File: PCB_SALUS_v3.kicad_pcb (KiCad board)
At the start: 2 copper layers, 100 x 100 mm, 85 parts, among them J1 Debug_U0, J10 RELES_2, J11 Throttle, J12 I2C_EXT1, J13 I2C_EXT2, J14 S_HALL, J15 RF_PPM, J16 USB_NATIVO, J17 SERVO2, J18 SERVO1, J19 +7V_IN, J2 S_GIRO, J20 3V_IN, J3 RS485, J4 Uart1, J5 5V_IN, J6 IBT_2, J7 FC1, J8 FC2, J9 RELES_1, U1 AMS1117CD-3.3, U2 SP3485EN, U4 BMI088, U5 74HC595, U6 ULN2003A, U7 LM358, U8 ESP32-S3-WROOM-1

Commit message: fixes
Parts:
- D1: value SM712_SOT23 -> SM712-02HTG
- moved D1 4.22 mm to (61.6, 117.8)
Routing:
- net /ESP32/RS485_A: track 11.2 -> 13.9 mm
- net /ESP32/RS485_B: track 14.6 -> 13.2 mm
- net GND: vias 11 -> 19

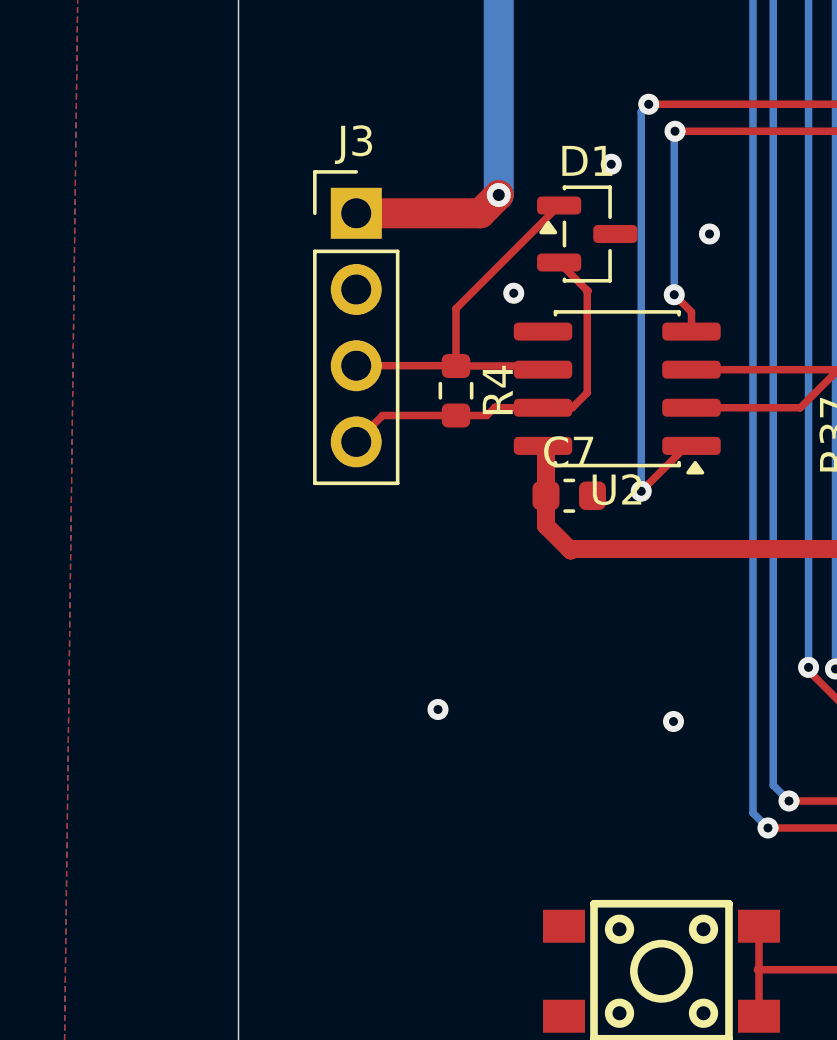
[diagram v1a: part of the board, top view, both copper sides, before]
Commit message: add second header for rs485
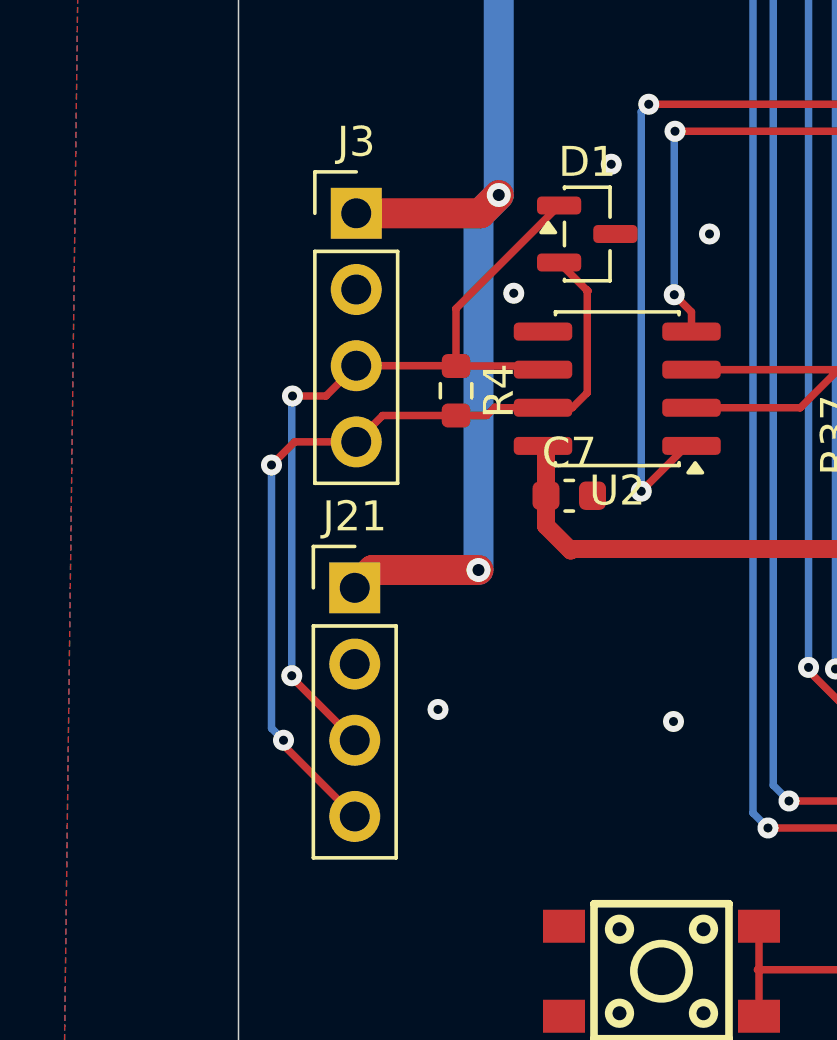
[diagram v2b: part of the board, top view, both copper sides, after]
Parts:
- added J21: RS485, Connector_PinHeader_2.54mm:PinHeader_1x04_P2.54mm_Vertical, F.Cu at (53.9, 129.6)
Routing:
- net +5V: track 264.9 -> 282.0 mm, vias 10 -> 11
- net /ESP32/RS485_B: track 13.2 -> 29.2 mm, vias 0 -> 2
- net /ESP32/RS485_A: track 13.9 -> 28.8 mm, vias 0 -> 2

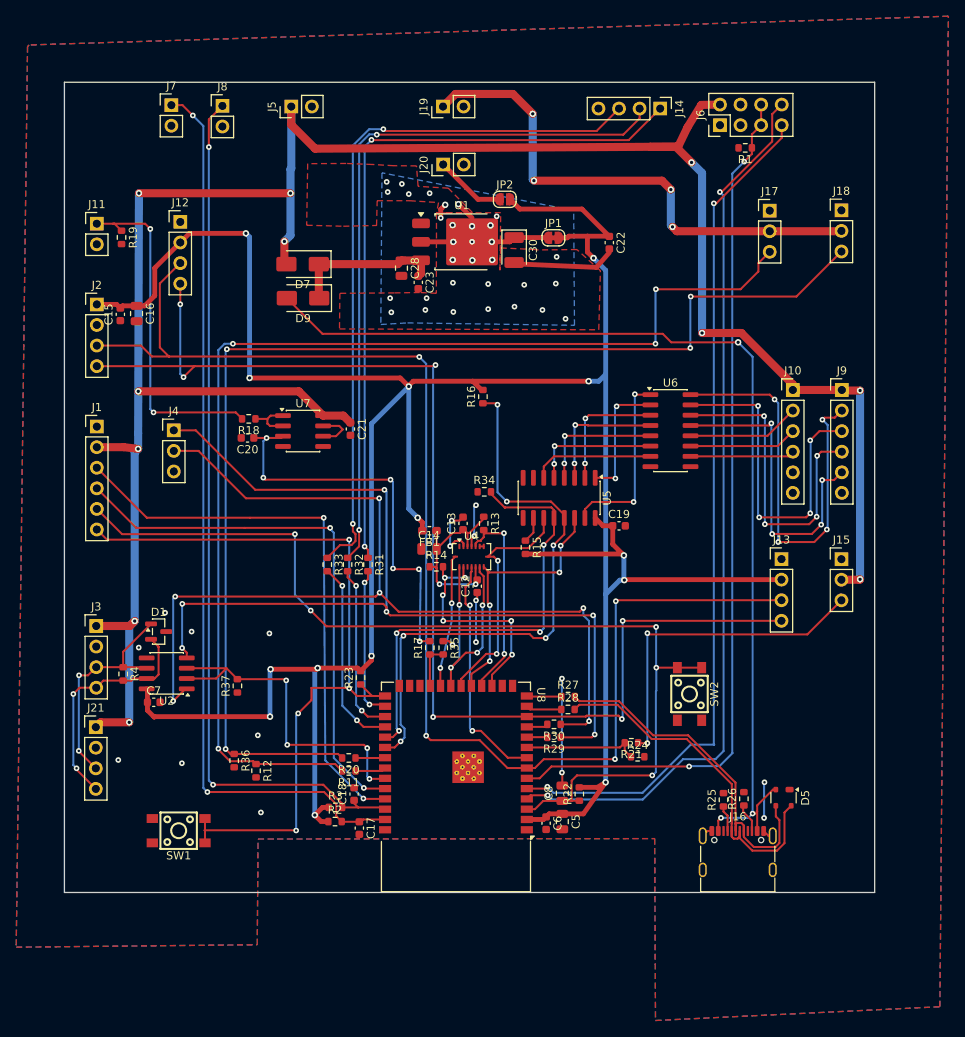
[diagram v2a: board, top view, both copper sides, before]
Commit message: vias de gnd y pin header de GPIOS sobrantes
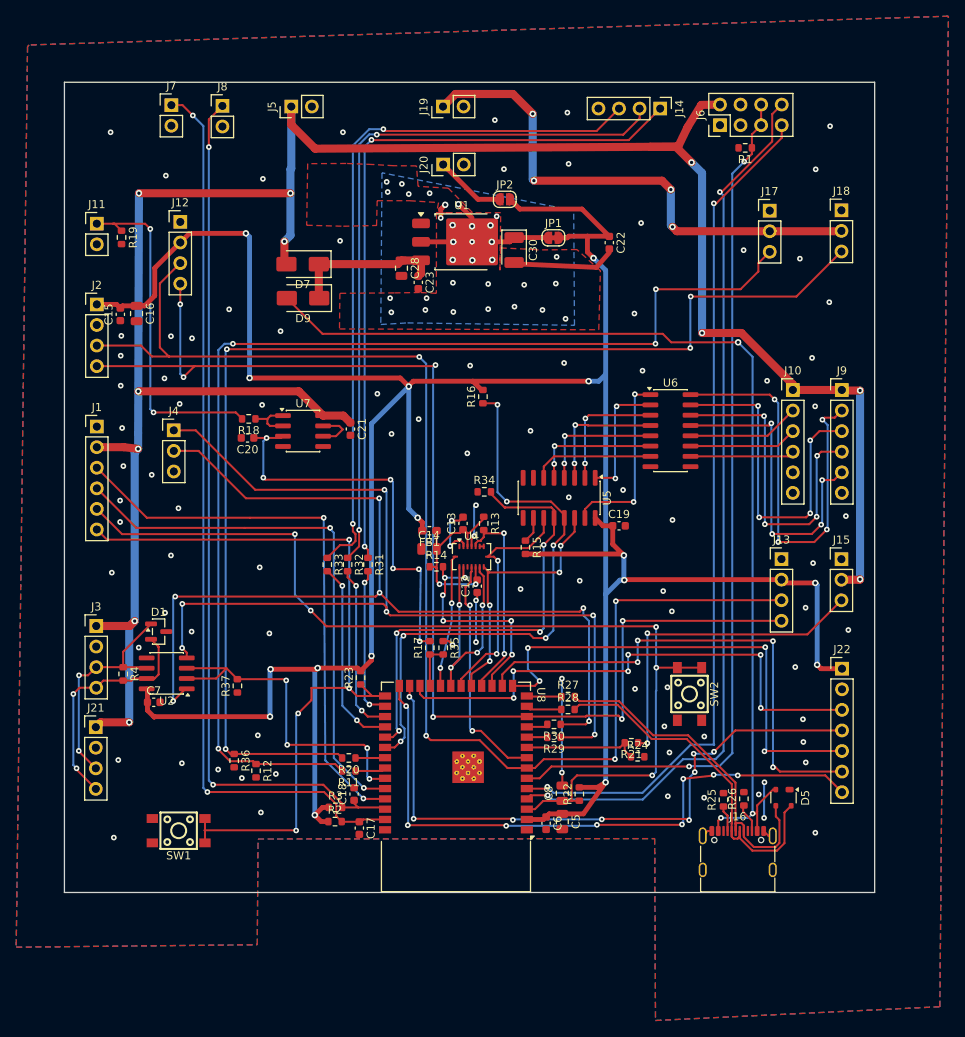
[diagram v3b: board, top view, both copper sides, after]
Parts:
- added J22: Conn_01x07, Connector_PinHeader_2.54mm:PinHeader_1x07_P2.54mm_Vertical, F.Cu at (146.0, 122.4)
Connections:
- U8 pad 15: unconnected-(U8-IO3-Pad15) -> /ESP32/IO3
- U8 pad 16: unconnected-(U8-IO46-Pad16) -> /ESP32/IO46
- U8 pad 24: unconnected-(U8-IO47-Pad24) -> /ESP32/IO47
- U8 pad 25: unconnected-(U8-IO48-Pad25) -> /ESP32/IO48
- U8 pad 26: unconnected-(U8-IO45-Pad26) -> /ESP32/IO45
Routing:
- net /ESP32/IO48: track 0.00 -> 78.9 mm, vias 0 -> 8
- net /ESP32/IO45: track 0.00 -> 77.9 mm, vias 0 -> 8
- net /ESP32/IO47: track 0.00 -> 65.4 mm, vias 0 -> 6
- net /ESP32/IO46: track 0.00 -> 62.5 mm, vias 0 -> 4
- net /ESP32/IO3: track 0.00 -> 60.2 mm, vias 0 -> 4
- net +3.3V: track 351.9 -> 369.7 mm, vias 14 -> 16
- net GND: vias 19 -> 93

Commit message: Mejora serigrafia profesional SALUS v3
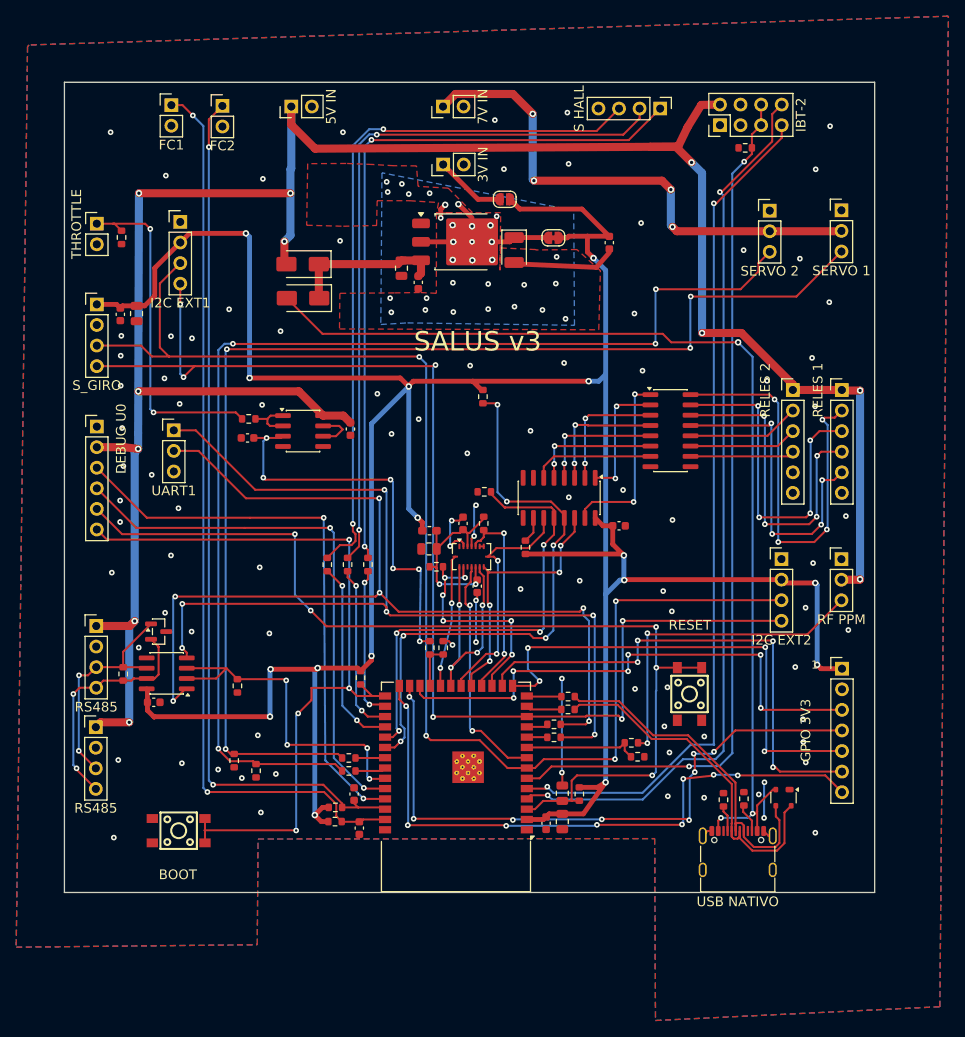
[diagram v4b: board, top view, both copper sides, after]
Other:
- board text added: "1"
- board text added: "3V IN"
- board text added: "5V IN"
- board text added: "7V IN"
- board text added: "BOOT"
- board text added: "DEBUG U0"
- board text added: "GPIO 3V3"
- board text added: "I2C EXT1"
- board text added: "I2C EXT2"
- board text added: "IBT-2"
- board text added: "RELES 1"
- board text added: "RELES 2"
- board text added: "RESET"
- board text added: "RF PPM"
- board text added: "S HALL"
- board text added: "SALUS v3"
- board text added: "SERVO 1"
- board text added: "SERVO 2"
- board text added: "THROTTLE"
- board text added: "UART1"
- board text added: "USB NATIVO"

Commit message: Identifica pines criticos de conectores
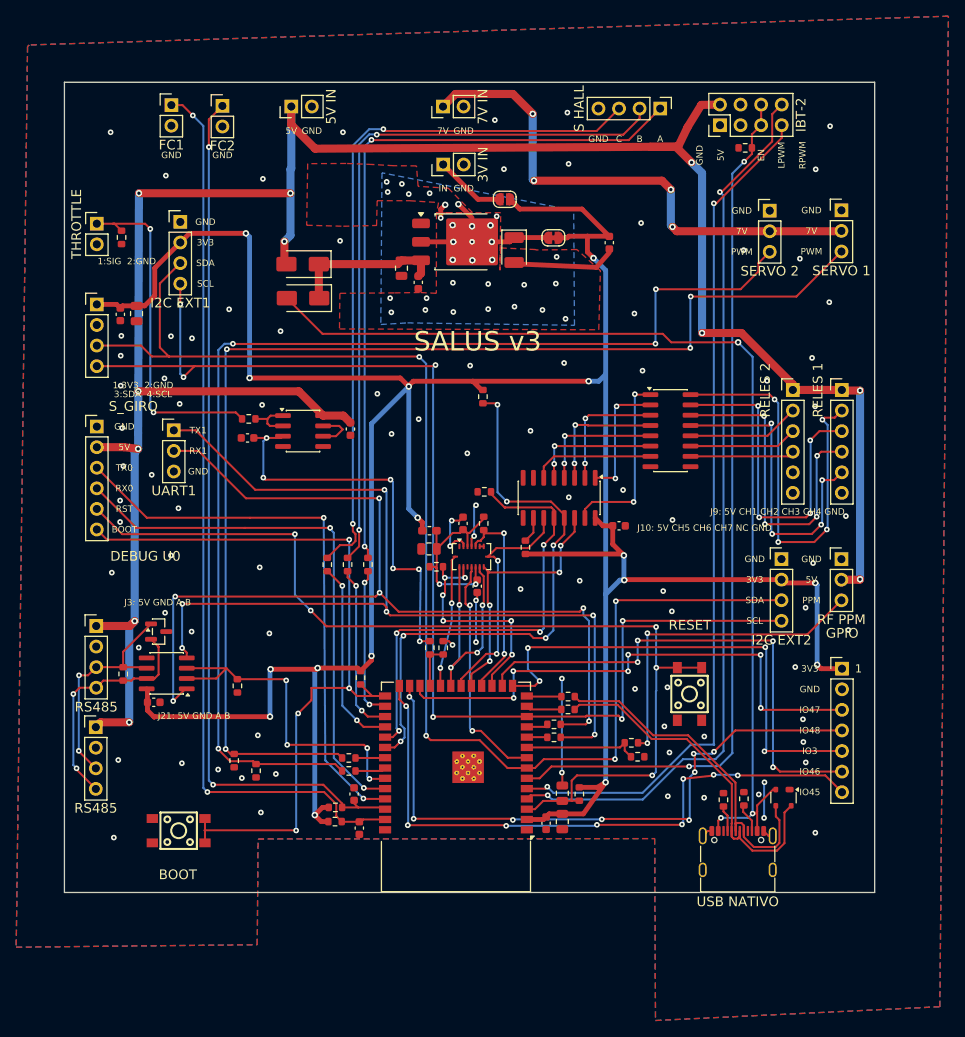
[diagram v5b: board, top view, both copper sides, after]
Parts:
- J22: value Conn_01x07 -> GPIOS_AUX
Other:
- board text added: "1:3V3 2:GND"
- board text added: "1:SIG 2:GND"
- board text added: "3:SDA 4:SCL"
- board text added: "3V3"
- board text added: "5V"
- board text added: "7V"
- board text added: "A"
- board text added: "B"
- board text added: "C"
- board text added: "EN"
- board text added: "GND"
- board text added: "GPIO"
- board text added: "IN"
- board text added: "IO3"
- board text added: "IO45"
- board text added: "IO46"
- board text added: "IO47"
- board text added: "IO48"
- board text added: "J10: 5V CH5 CH6 CH7 NC GND"
- board text added: "J21: 5V GND A B"
- board text added: "J3: 5V GND A B"
- board text added: "J9: 5V CH1 CH2 CH3 CH4 GND"
- board text added: "LPWM"
- board text added: "PPM"
- board text added: "PWM"
- board text added: "RPWM"
- board text added: "RST"
- board text added: "RX0"
- board text added: "RX1"
- board text added: "SCL"
- board text added: "SDA"
- board text added: "TX0"
- board text added: "TX1"
- board text removed: "GPIO 3V3"

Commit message: Libera paquete JLCPCB SALUS v3
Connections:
- net Net-(J20-Pin_1) renamed /ALIMENTACION/3.3V_EXT
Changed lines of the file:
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@@
 			(size 1 0.5)
 			(layers "F.Cu" "F.Mask")
-			(net "Net-(J20-Pin_1)")
+			(net "/ALIMENTACION/3.3V_EXT")
 			(pinfunction "A_1")
 			(pintype "passive")
@@
 			(layers "*.Cu" "*.Mask")
 			(remove_unused_layers no)
-			(net "Net-(J20-Pin_1)")
+			(net "/ALIMENTACION/3.3V_EXT")
 			(pinfunction "Pin_1_1")
 			(pintype "passive")
@@
 	)
 	(segment
-		(start 96.745 60.155)
-		(end 101.04 64.45)
-		(width 0.6)
-		(layer "F.Cu")
-		(net "Net-(J20-Pin_1)")
-	)
-	(segment
-		(start 101.04 64.45)
-		(end 103.7 64.45)
-		(width 0.6)
-		(layer "F.Cu")
-		(net "Net-(J20-Pin_1)")
-	)
-	(segment
 		(start 104.6 101.75)
 		(end 110.053408 101.75)
@@
 		(net "Net-(U7B--)")
 	)
+	(segment
+		(start 96.745 60.155)
+		(end 101.04 64.45)
+		(width 0.6)
+		(layer "F.Cu")
+		(net "/ALIMENTACION/3.3V_EXT")
+	)
+	(segment
+		(start 101.04 64.45)
+		(end 103.7 64.45)
+		(width 0.6)
+		(layer "F.Cu")
+		(net "/ALIMENTACION/3.3V_EXT")
+	)
 	(zone
